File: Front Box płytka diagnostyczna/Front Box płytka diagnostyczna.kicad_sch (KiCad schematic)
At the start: 7 parts

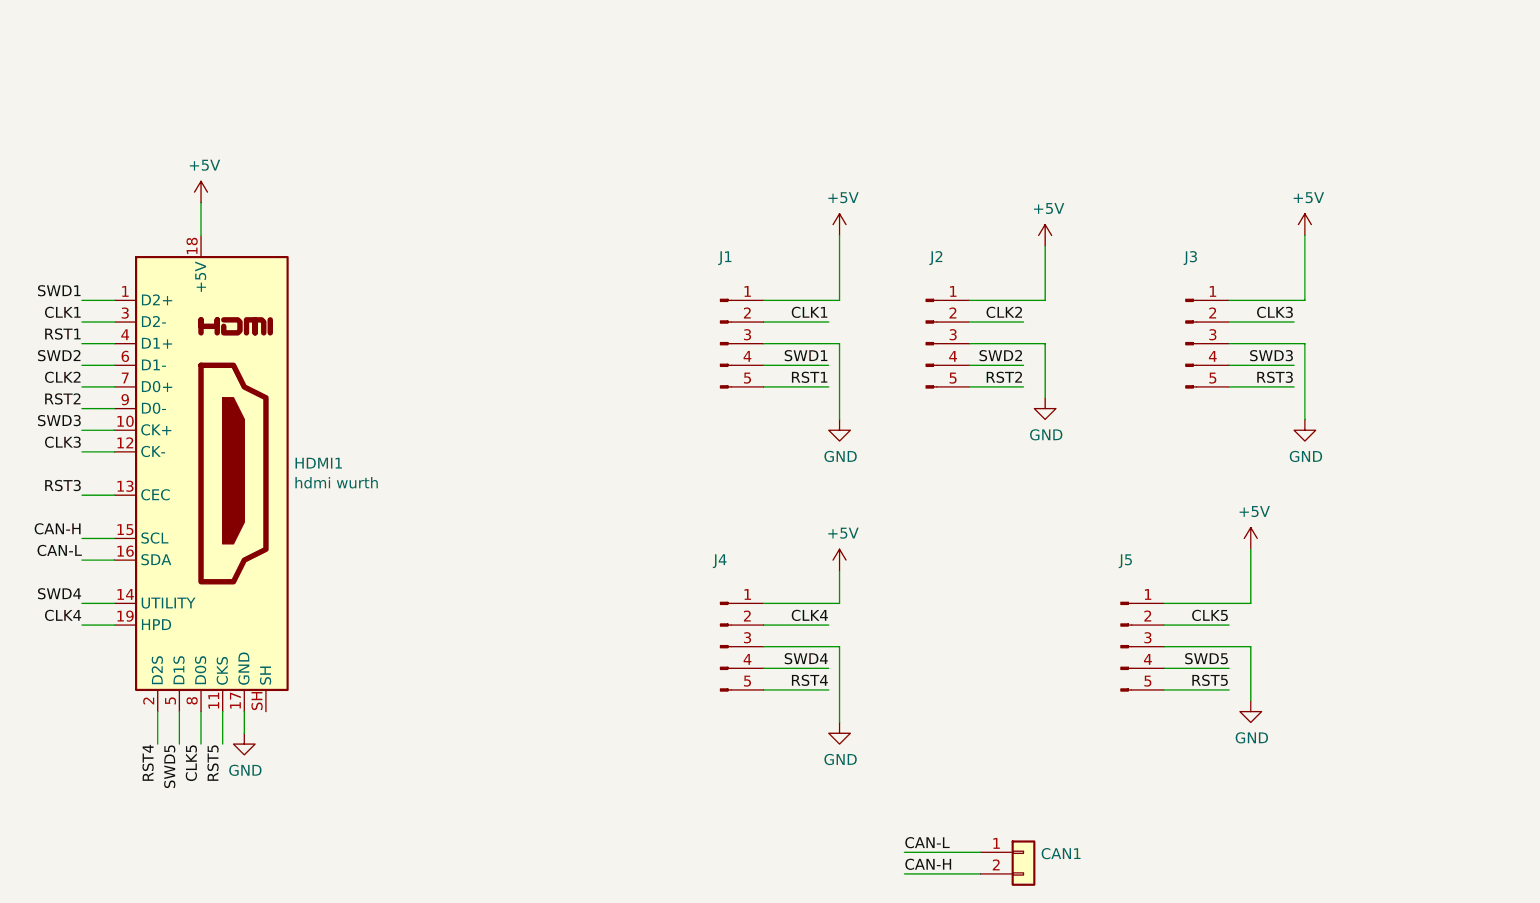
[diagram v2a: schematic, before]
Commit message: quick revision
Added LED's to horizontal board, distance between sockets fix, Diagnostic Board 5v line delete and compatibility with HDMI fix
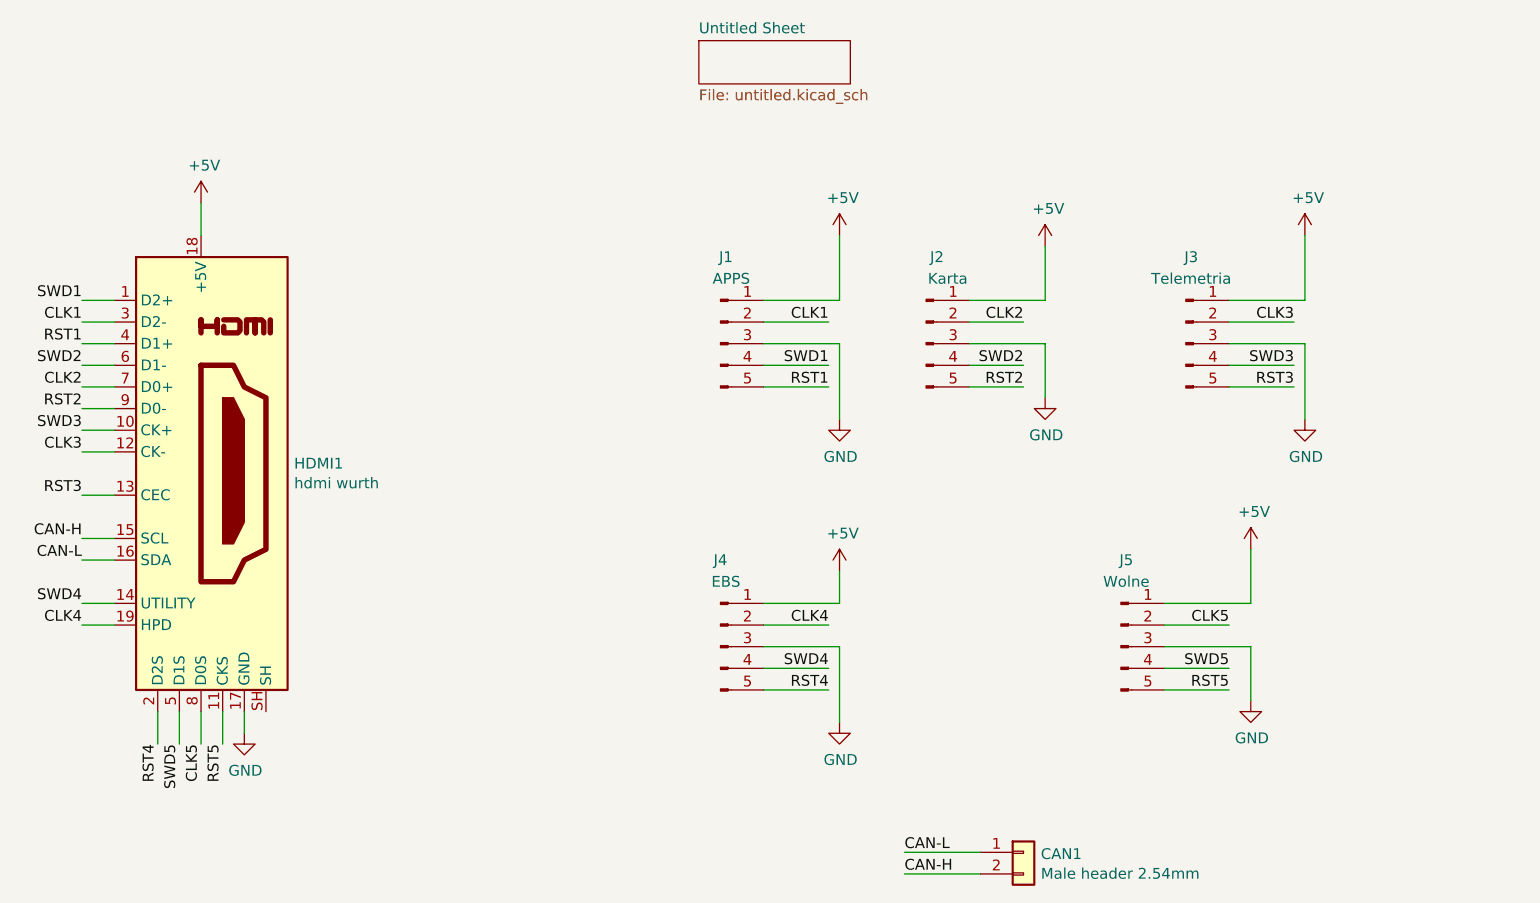
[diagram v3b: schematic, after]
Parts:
- CAN1: value (none) -> Male header 2.54mm
- J1: value (none) -> APPS; footprint (none) -> Connector_PinHeader_2.54mm:PinHeader_1x05_P2.54mm_Vertical
- J2: value (none) -> Karta; footprint (none) -> Connector_PinHeader_2.54mm:PinHeader_1x05_P2.54mm_Vertical
- J3: value (none) -> Telemetria; footprint (none) -> Connector_PinHeader_2.54mm:PinHeader_1x05_P2.54mm_Vertical
- J4: value (none) -> EBS; footprint (none) -> Connector_PinHeader_2.54mm:PinHeader_1x05_P2.54mm_Vertical
- J5: value (none) -> Wolne; footprint (none) -> Connector_PinHeader_2.54mm:PinHeader_1x05_P2.54mm_Vertical
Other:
- added sheet Untitled Sheet (untitled.kicad_sch)
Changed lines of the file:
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@@
     (in_bom yes) (on_board yes) (fields_autoplaced)
     (property "Reference" "J5" (id 0) (at 184.785 100.33 0))
-    (property "Value" "" (id 1) (at 184.785 102.87 0))
-    (property "Footprint" "" (id 2) (at 184.15 110.49 0)
+    (property "Value" "Wolne" (id 1) (at 184.785 102.87 0))
+    (property "Footprint" "Connector_PinHeader_2.54mm:PinHeader_1x05_P2.54mm_Vertical" (id 2) (at 184.15 110.49 0)
       (effects (font (size 1.27 1.27)) hide)
     )
@@
     (in_bom yes) (on_board yes)
     (property "Reference" "J4" (id 0) (at 137.16 100.33 0))
-    (property "Value" "" (id 1) (at 137.795 102.87 0))
-    (property "Footprint" "" (id 2) (at 137.16 110.49 0)
+    (property "Value" "EBS" (id 1) (at 137.795 102.87 0))
+    (property "Footprint" "Connector_PinHeader_2.54mm:PinHeader_1x05_P2.54mm_Vertical" (id 2) (at 137.16 110.49 0)
       (effects (font (size 1.27 1.27)) hide)
     )
@@
       (effects (font (size 1.27 1.27)) (justify left))
     )
-    (property "Value" "" (id 1) (at 174.752 137.1346 0)
+    (property "Value" "Male header 2.54mm" (id 1) (at 174.752 137.1346 0)
       (effects (font (size 1.27 1.27)) (justify left))
     )
@@
     (in_bom yes) (on_board yes)
     (property "Reference" "J2" (id 0) (at 162.56 64.77 0))
-    (property "Value" "" (id 1) (at 163.83 67.31 0))
-    (property "Footprint" "" (id 2) (at 161.29 74.93 0)
+    (property "Value" "Karta" (id 1) (at 163.83 67.31 0))
+    (property "Footprint" "Connector_PinHeader_2.54mm:PinHeader_1x05_P2.54mm_Vertical" (id 2) (at 161.29 74.93 0)
       (effects (font (size 1.27 1.27)) hide)
     )
@@
     (in_bom yes) (on_board yes) (fields_autoplaced)
     (property "Reference" "J3" (id 0) (at 192.405 64.77 0))
-    (property "Value" "" (id 1) (at 192.405 67.31 0))
-    (property "Footprint" "" (id 2) (at 191.77 74.93 0)
+    (property "Value" "Telemetria" (id 1) (at 192.405 67.31 0))
+    (property "Footprint" "Connector_PinHeader_2.54mm:PinHeader_1x05_P2.54mm_Vertical" (id 2) (at 191.77 74.93 0)
       (effects (font (size 1.27 1.27)) hide)
     )
@@
     (in_bom yes) (on_board yes)
     (property "Reference" "J1" (id 0) (at 137.795 64.77 0))
-    (property "Value" "" (id 1) (at 138.43 67.31 0))
-    (property "Footprint" "" (id 2) (at 137.16 74.93 0)
+    (property "Value" "APPS" (id 1) (at 138.43 67.31 0))
+    (property "Footprint" "Connector_PinHeader_2.54mm:PinHeader_1x05_P2.54mm_Vertical" (id 2) (at 137.16 74.93 0)
       (effects (font (size 1.27 1.27)) hide)
     )
@@
     (pin "1")
   )
+  (sheet (at 134.62 39.37) (size 17.78 5.08) (fields_autoplaced)
+    (stroke (width 0.1524) (type solid) (color 0 0 0 0))
+    (fill (color 0 0 0 0.0000))
+    (property "Sheet name" "Untitled Sheet" (id 0) (at 134.62 38.6584 0)
+      (effects (font (size 1.27 1.27)) (justify left bottom))
+    )
+    (property "Sheet file" "untitled.kicad_sch" (id 1) (at 134.62 45.0346 0)
+      (effects (font (size 1.27 1.27)) (justify left top))
+    )
+  )
   (sheet_instances
     (path "/" (page "1"))
+    (path "/3742a313-c63e-4807-a7bf-be5a0ae2c781" (page "2"))
   )
   (symbol_instances
@@
       (reference "#PWR0112") (unit 1) (value "+5V") (footprint "")
     )
+    (path "/3742a313-c63e-4807-a7bf-be5a0ae2c781/4fe6981b-b29c-4bff-8414-9cf327d56d31"
+      (reference "#PWR?") (unit 1) (value "+3.3V") (footprint "")
+    )
     (path "/356199c8-c0f7-4995-bef0-53ad752a30c5"
       (reference "CAN1") (unit 1) (value "Male header 2.54mm") (footprint "Connector_PinHeader_2.54mm:PinHeader_1x02_P2.54mm_Vertical")
     )
+    (path "/3742a313-c63e-4807-a7bf-be5a0ae2c781/79fa2112-ba21-4d8b-a179-bbafcafc0b2a"
+      (reference "D?") (unit 1) (value "LED") (footprint "")
+    )
     (path "/08ac4c42-16f0-4513-b91e-bf0b3a111257"
       (reference "HDMI1") (unit 1) (value "hdmi wurth") (footprint "footprints:685119134923")
@@
       (reference "J5") (unit 1) (value "Wolne") (footprint "Connector_PinHeader_2.54mm:PinHeader_1x05_P2.54mm_Vertical")
     )
-  )
+    (path "/3742a313-c63e-4807-a7bf-be5a0ae2c781/0ee4f337-95e5-4a44-a816-f788821cba4a"
+      (reference "R?") (unit 1) (value "R") (footprint "")
+    )
+    (path "/3742a313-c63e-4807-a7bf-be5a0ae2c781/2361ed9d-44ac-40c1-ab71-db1419d4ef87"
+      (reference "U?") (unit 1) (value "MCP2562-E-SN") (footprint "Package_SO:SOIC-8_3.9x4.9mm_P1.27mm")
+    )
+  )
